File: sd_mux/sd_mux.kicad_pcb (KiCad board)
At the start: 2 copper layers, 77.5 x 38.1 mm, 16 parts, among them IC1 SN74CBT3257DR, IC2 SN74CBT3257DR, J1 Micro_SD_Card_Det, J2 DEVICE 1, J3 DEVICE 2, J4 CONTROL

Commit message: routed
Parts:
- moved R4 44.7 mm to (148.6, 73.7)
- moved LED2 44.7 mm to (153.7, 73.7)
- moved R3 44.6 mm to (148.6, 77.5)
- moved LED1 44.6 mm to (153.7, 77.5)
- moved J4 43.2 mm to (158.8, 83.8)
- moved R1 43.2 mm to (160.0, 87.6)
- moved C1 34.2 mm to (133.3, 72.4), turned to 180 degrees
- moved J1 27.9 mm to (113.0, 72.4)
- moved R5 27.7 mm to (133.3, 108.0), turned to 180 degrees
- moved IC1 23.4 mm to (133.3, 80.0), turned to 270 degrees
- moved IC2 18.0 mm to (133.3, 100.3), turned to 270 degrees
- moved J3 15.3 mm to (110.5, 99.1)
- moved J2 12.0 mm to (161.3, 99.1)
- moved C2 11.4 mm to (133.3, 92.7), turned to 180 degrees
- moved C3 10.5 mm to (121.9, 73.7)
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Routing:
- net GND: track 0.00 -> 241.5 mm, vias 0 -> 18
- net DAT2_1: track 0.00 -> 56.2 mm, vias 0 -> 2
- net VCC: track 13.9 -> 70.1 mm
- net DAT3/CD_1: track 0.00 -> 53.2 mm, vias 0 -> 2
- net Net-(IC1-Pad4): track 68.1 -> 19.2 mm
- net VDD_1: track 0.00 -> 44.3 mm, vias 0 -> 2
- net CMD_1: track 0.00 -> 40.2 mm, vias 0 -> 2
- net Net-(IC1-Pad7): track 56.5 -> 21.9 mm
- net DAT1_2: track 0.00 -> 32.1 mm, vias 0 -> 2
- net DAT0_2: track 0.00 -> 25.9 mm, vias 0 -> 2
- net Net-(IC1-Pad9): track 52.4 -> 31.8 mm, vias 0 -> 2
- net CLK_2: track 0.00 -> 20.6 mm, vias 0 -> 2
- net VDD_2: track 22.7 -> 40.3 mm, vias 2 -> 4
- net OE: track 43.4 -> 27.8 mm, vias 3 -> 2
- net Net-(IC2-Pad12): track 32.2 -> 47.5 mm, vias 2 -> 4
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- added copper zone on B.Cu, net GND
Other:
- board size 77.5 x 38.1 mm -> 63.5 x 38.1 mm

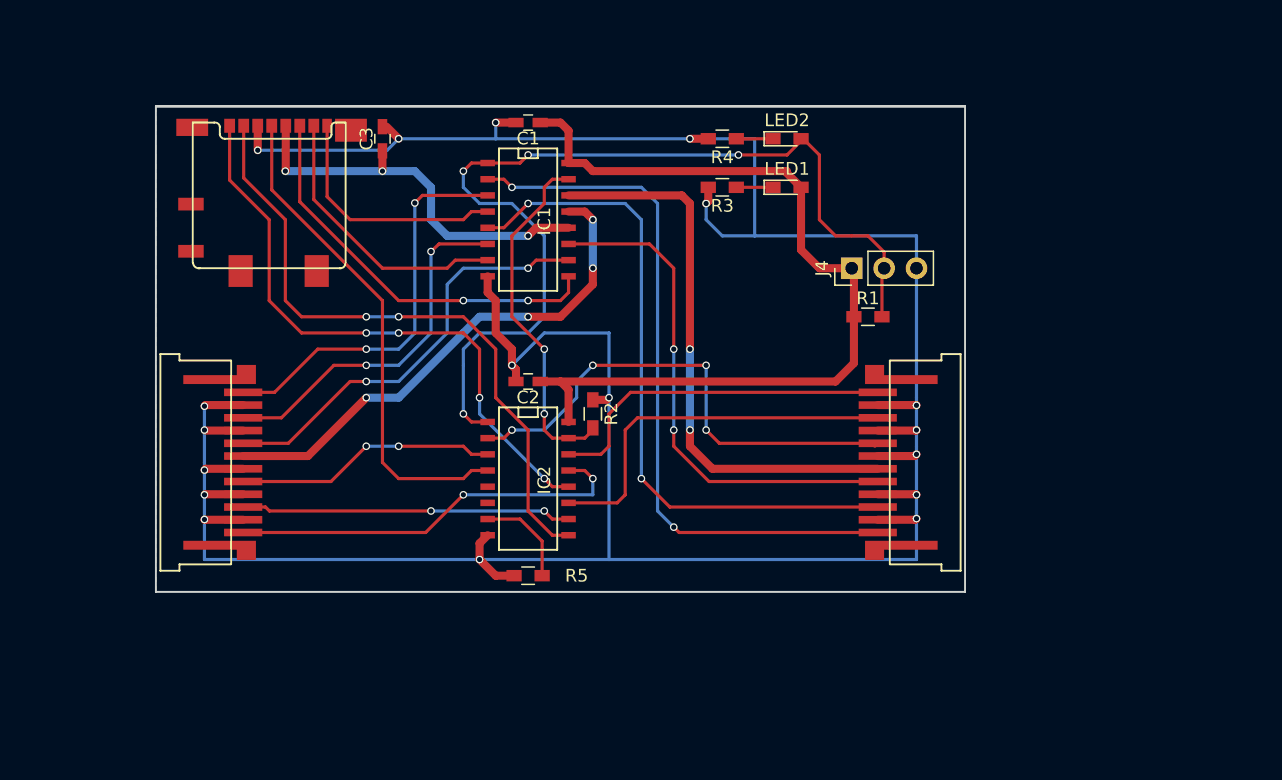
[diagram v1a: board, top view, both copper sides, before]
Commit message: redid the mux board in the same form factor as the beaglebone black, started work on sd plug board
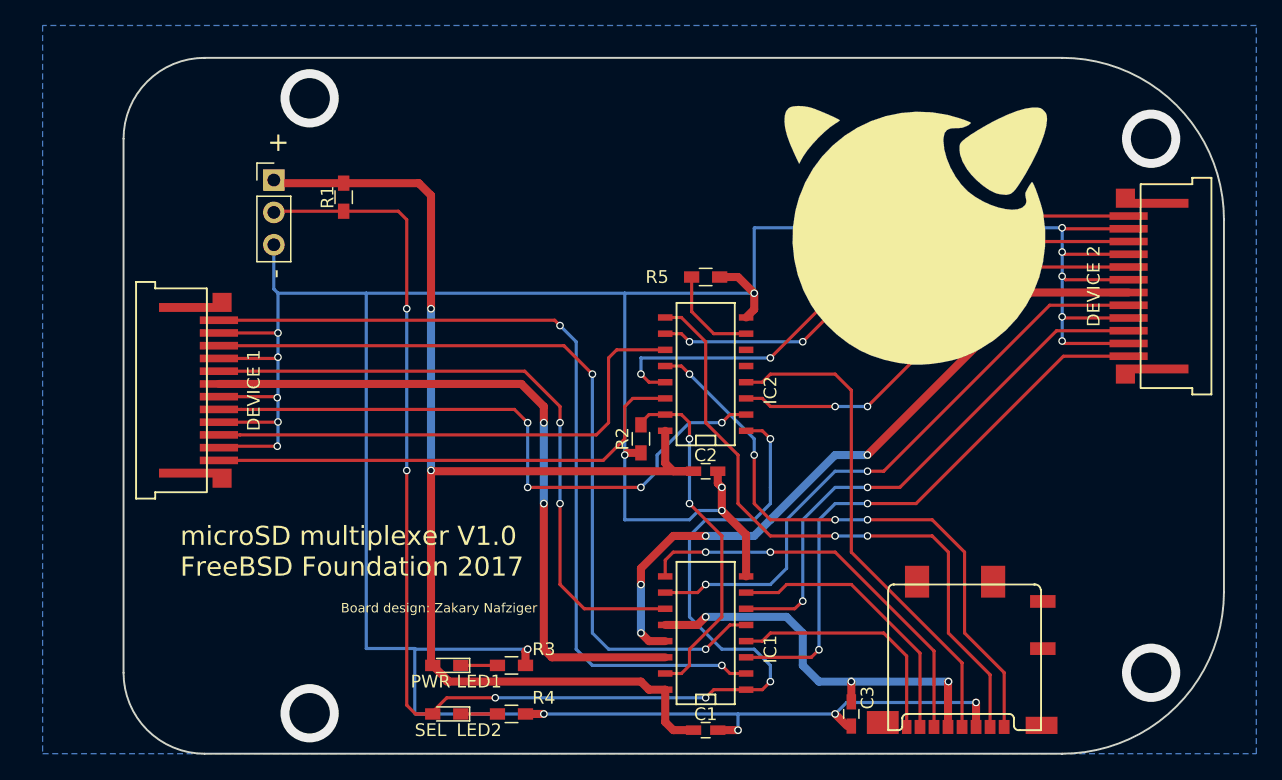
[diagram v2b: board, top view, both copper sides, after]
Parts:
- added G***: LOGO, sd_mux_footprints:fbsd_logo, B.Cu at (146.1, 94.0)
- added G***: LOGO, sd_mux_footprints:fbsd_logo, F.Cu at (163.8, 81.3)
- moved J1 72.5 mm to (167.6, 120.1), turned to 0 degrees
- moved J3 71.8 mm to (181.0, 85.2), turned to 90 degrees
- moved C3 58.2 mm to (158.7, 118.8), turned to 270 degrees
- moved J2 53.0 mm to (108.6, 93.4), turned to 270 degrees
- moved LED2 52.4 mm to (127.0, 118.8), turned to 180 degrees
- moved C1 49.7 mm to (147.3, 120.1), turned to 0 degrees
- moved R4 48.1 mm to (132.0, 118.8), turned to 0 degrees
- moved LED1 46.1 mm to (127.0, 115.0), turned to 180 degrees
- moved J4 45.9 mm to (113.4, 76.9), turned to 0 degrees
- moved R1 42.2 mm to (118.9, 78.2), turned to 270 degrees
- moved R3 41.0 mm to (132.0, 115.0), turned to 0 degrees
- moved IC1 35.3 mm to (147.3, 112.5), turned to 90 degrees
- moved R5 27.3 mm to (147.3, 84.5), turned to 0 degrees
- moved IC2 16.2 mm to (147.3, 92.1), turned to 90 degrees
- moved C2 15.6 mm to (147.3, 99.8), turned to 0 degrees
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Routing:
- net GND: track 241.5 -> 282.1 mm, vias 18 -> 19
- net device_select: track 76.2 -> 109.2 mm, vias 4 -> 6
- net VCC: track 70.1 -> 99.8 mm, vias 0 -> 2
- net VDD_2: track 40.3 -> 54.5 mm
- net DAT2_2: track 31.6 -> 45.8 mm
- net DAT1_2: track 32.1 -> 46.3 mm
- net CLK_2: track 20.6 -> 34.8 mm
- net DAT3/CD_2: track 28.6 -> 42.8 mm
- net CMD_2: track 33.7 -> 47.9 mm
- net DAT0_2: track 25.9 -> 39.9 mm
- net DAT0_1: track 30.0 -> 40.8 mm
- net VDD_1: track 44.3 -> 55.1 mm
- net CMD_1: track 40.2 -> 50.9 mm
- net DAT1_1: track 27.8 -> 38.5 mm
- net DAT2_1: track 56.2 -> 67.0 mm
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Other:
- board size 63.5 x 38.1 mm -> 86.4 x 54.6 mm
- rule pad_to_mask_clearance: 0.2 -> 0
- board text added: "+"
- board text added: "-"
- board text added: "Board design: Zakary Nafziger"
- board text added: "microSD multiplexer V1.0 FreeBSD Foundation 2017"

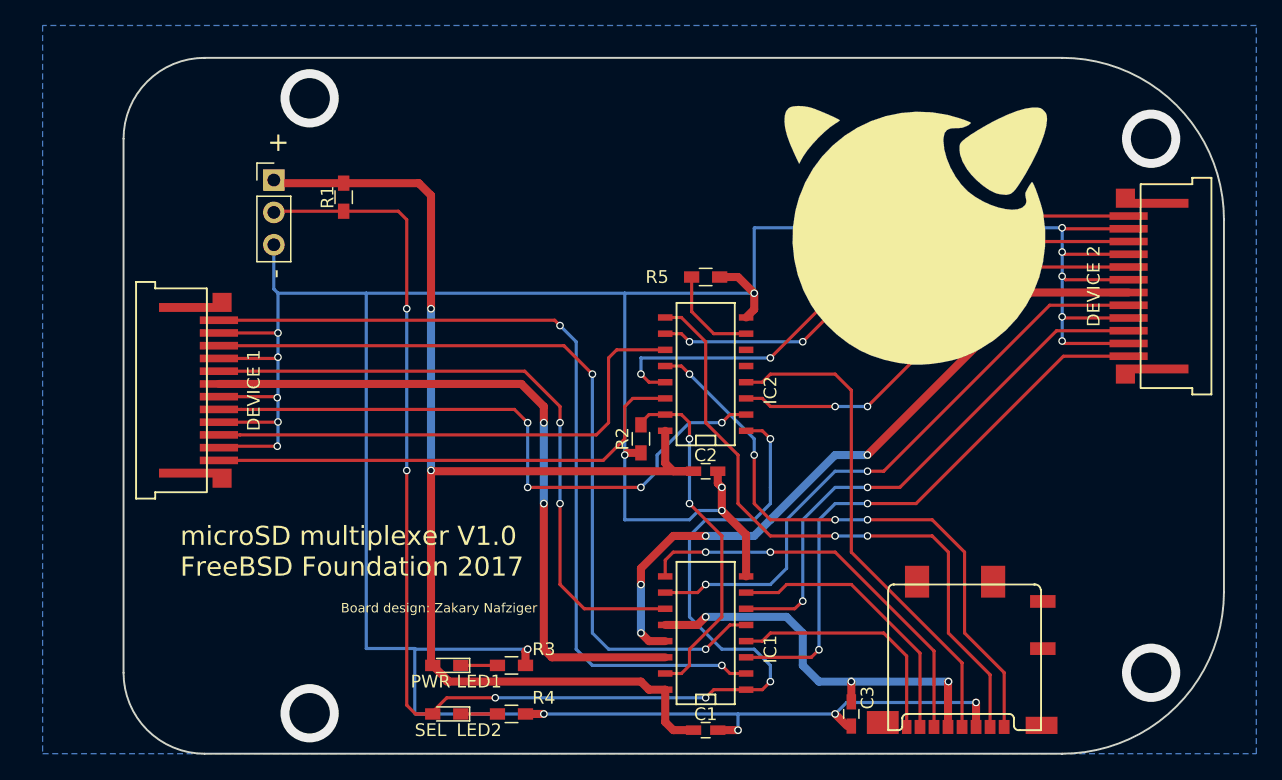
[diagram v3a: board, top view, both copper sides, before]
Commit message: redid mounting holes on mux board
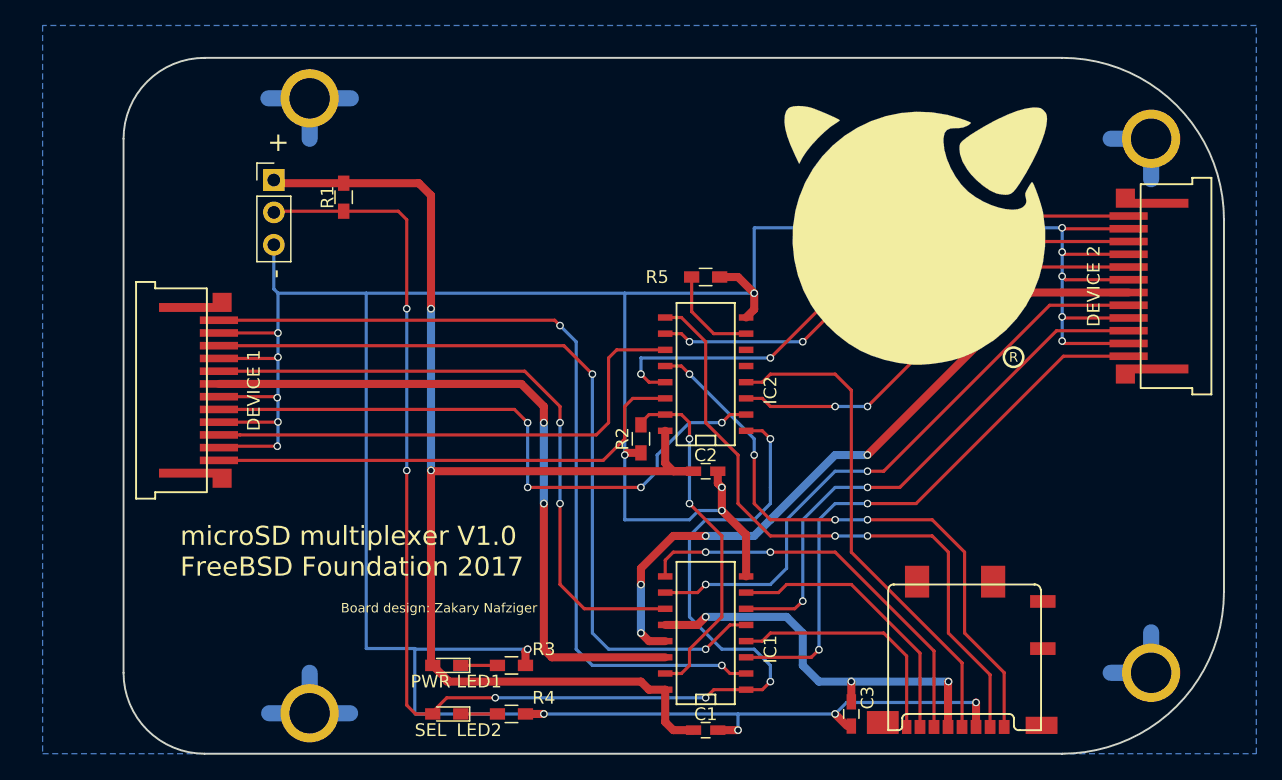
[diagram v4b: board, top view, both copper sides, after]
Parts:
- added REF**: 125mil_plated_mounting_hole, sd_mux_footprints:125mil_plated_mounting_hole, F.Cu at (182.2, 73.7)
- added REF**: 125mil_plated_mounting_hole, sd_mux_footprints:125mil_plated_mounting_hole, F.Cu at (182.2, 115.6)
- added REF**: 125mil_plated_mounting_hole, sd_mux_footprints:125mil_plated_mounting_hole, F.Cu at (116.2, 118.7)
- added REF**: 125mil_plated_mounting_hole, sd_mux_footprints:125mil_plated_mounting_hole, F.Cu at (116.2, 70.5)
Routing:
- net (no net): track 0.00 -> 31.9 mm, vias 4 -> 0
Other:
- rule pad_to_mask_clearance: 0 -> 0.127
- board text added: "R"
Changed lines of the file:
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@@
 (kicad_pcb (version 4) (host pcbnew 4.0.7)
   (general
-    (links 57)
+    (links 0)
     (no_connects 0)
-    (area 101.524999 67.234999 188.035001 121.995001)
+    (area 95.25 64.77 193.614049 122.87)
     (thickness 1.6)
-    (drawings 12)
-    (tracks 385)
+    (drawings 16)
+    (tracks 391)
     (zones 0)
-    (modules 18)
+    (modules 22)
     (nets 31)
   )
@@
   )
   (setup
-    (last_trace_width 0.25)
+    (last_trace_width 1.27)
     (user_trace_width 0.635)
+    (user_trace_width 1.27)
     (trace_clearance 0.25)
     (zone_clearance 0.508)
@@
     (uvia_drill 0.1)
     (uvias_allowed no)
-    (uvia_min_size 0.2)
-    (uvia_min_drill 0.1)
+    (uvia_min_size 0)
+    (uvia_min_drill 0)
     (pcb_text_width 0.3)
     (pcb_text_size 1.5 1.5)
@@
     (pad_size 1.524 1.524)
     (pad_drill 0.762)
-    (pad_to_mask_clearance 0)
+    (pad_to_mask_clearance 0.127)
     (solder_mask_min_width 0.0254)
     (aux_axis_origin 0 0)
@@
       (padsonsilk false)
       (subtractmaskfromsilk false)
-      (outputformat 1)
+      (outputformat 4)
       (mirror false)
       (drillshape 0)
       (scaleselection 1)
-      (outputdirectory gerbers/))
+      (outputdirectory ../../pdfs/sd_mux/))
   )
   (net 0 "")
@@
     (add_net device_select)
   )
+  (module sd_mux_footprints:125mil_plated_mounting_hole (layer F.Cu)
+    (at 182.245 73.66)
+    (fp_text reference REF** (at 0 3) (layer F.SilkS) hide
+      (effects (font (size 1 1) (thickness 0.15)))
+    )
+    (fp_text value 125mil_plated_mounting_hole (at 0 -3) (layer F.Fab)
+      (effects (font (size 1 1) (thickness 0.15)))
+    )
+    (pad 1 thru_hole circle (at 0 0) (size 4.572 4.572) (drill 3.175) (layers *.Cu *.Mask))
+  )
+  (module sd_mux_footprints:125mil_plated_mounting_hole (layer F.Cu)
+    (at 182.245 115.57)
+    (fp_text reference REF** (at 0 3) (layer F.SilkS) hide
+      (effects (font (size 1 1) (thickness 0.15)))
+    )
+    (fp_text value 125mil_plated_mounting_hole (at 0 -3) (layer F.Fab)
+      (effects (font (size 1 1) (thickness 0.15)))
+    )
+    (pad 1 thru_hole circle (at 0 0) (size 4.572 4.572) (drill 3.175) (layers *.Cu *.Mask))
+  )
+  (module sd_mux_footprints:125mil_plated_mounting_hole (layer F.Cu)
+    (at 116.205 118.745)
+    (fp_text reference REF** (at 0 3) (layer F.SilkS) hide
+      (effects (font (size 1 1) (thickness 0.15)))
+    )
+    (fp_text value 125mil_plated_mounting_hole (at 0 -3) (layer F.Fab)
+      (effects (font (size 1 1) (thickness 0.15)))
+    )
+    (pad 1 thru_hole circle (at 0 0) (size 4.572 4.572) (drill 3.175) (layers *.Cu *.Mask))
+  )
   (module sd_mux_footprints:fbsd_logo (layer B.Cu)
     (at 146.05 93.98 180)
@@
       (xy -9.657279 -10.166238) (xy -9.282257 -10.193894) (xy -8.854976 -10.171624)) (layer F.SilkS) (width 0.01))
   )
+  (module sd_mux_footprints:125mil_plated_mounting_hole (layer F.Cu)
+    (at 116.205 70.485)
+    (fp_text reference REF** (at 0 3) (layer F.SilkS) hide
+      (effects (font (size 1 1) (thickness 0.15)))
+    )
+    (fp_text value 125mil_plated_mounting_hole (at 0 -3) (layer F.Fab)
+      (effects (font (size 1 1) (thickness 0.15)))
+    )
+    (pad 1 thru_hole circle (at 0 0) (size 4.572 4.572) (drill 3.175) (layers *.Cu *.Mask))
+  )
+  (gr_text R (at 138.43 103.505) (layer B.SilkS)
+    (effects (font (size 0.762 0.762) (thickness 0.1905)) (justify mirror))
+  )
+  (gr_circle (center 138.43 103.505) (end 137.668 103.505) (layer B.SilkS) (width 0.2))
+  (gr_circle (center 171.45 90.805) (end 170.688 90.805) (layer F.SilkS) (width 0.2))
+  (gr_text R (at 171.45 90.805) (layer F.SilkS)
+    (effects (font (size 0.762 0.762) (thickness 0.1905)))
+  )
   (gr_text "Board design: Zakary Nafziger" (at 126.365 110.49) (layer F.SilkS)
     (effects (font (size 0.738 0.738) (thickness 0.1845)))
@@
     (effects (font (size 1.5 1.5) (thickness 0.3)))
   )
-  (via (at 182.245 73.66) (size 4.572) (drill 3.175) (layers F.Cu B.Cu) (net 0))
-  (via (at 182.245 115.57) (size 4.572) (drill 3.175) (layers F.Cu B.Cu) (net 0))
-  (via (at 116.205 118.745) (size 4.572) (drill 3.175) (layers F.Cu B.Cu) (net 0))
-  (via (at 116.205 70.485) (size 4.572) (drill 3.175) (layers F.Cu B.Cu) (net 0))
+  (segment (start 182.245 73.66) (end 182.245 76.835) (width 1.27) (layer B.Cu) (net 0))
+  (segment (start 182.245 73.66) (end 179.07 73.66) (width 1.27) (layer B.Cu) (net 0))
+  (segment (start 182.245 115.57) (end 182.245 112.395) (width 1.27) (layer B.Cu) (net 0))
+  (segment (start 182.245 115.57) (end 179.07 115.57) (width 1.27) (layer B.Cu) (net 0))
+  (segment (start 116.205 118.745) (end 119.38 118.745) (width 1.27) (layer B.Cu) (net 0))
+  (segment (start 116.205 118.745) (end 116.205 115.57) (width 1.27) (layer B.Cu) (net 0))
+  (segment (start 116.205 118.745) (end 113.03 118.745) (width 1.27) (layer B.Cu) (net 0))
+  (segment (start 116.205 70.485) (end 116.205 73.66) (width 1.27) (layer B.Cu) (net 0))
+  (segment (start 116.205 70.485) (end 119.437892 70.485) (width 1.27) (layer B.Cu) (net 0))
+  (segment (start 116.205 70.485) (end 112.972108 70.485) (width 1.27) (layer B.Cu) (net 0))
   (segment (start 125.73 78.105) (end 124.771778 77.146778) (width 0.635) (layer F.Cu) (net 1))
   (segment (start 124.771778 77.146778) (end 118.876266 77.146778) (width 0.635) (layer F.Cu) (net 1))

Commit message: rerouted mux board to fix FFC flip issue and fix tracks that had become unalaigned from the grid
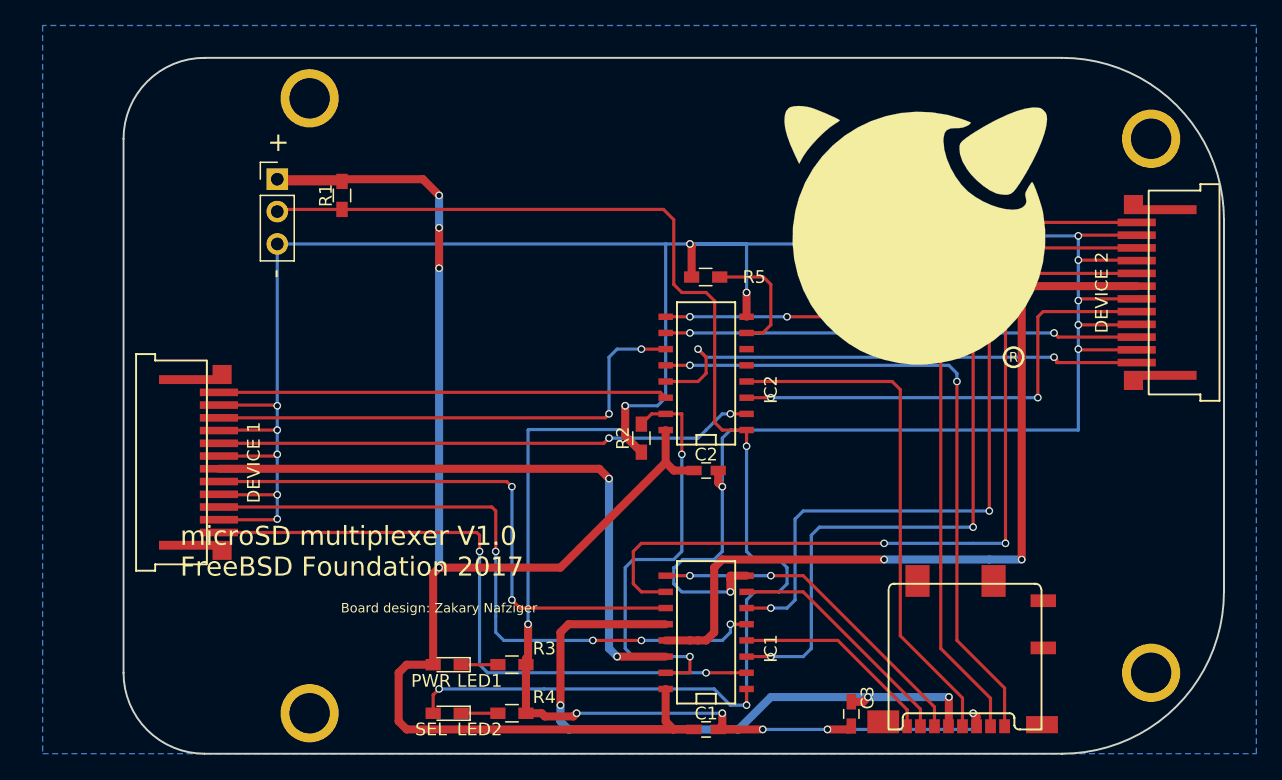
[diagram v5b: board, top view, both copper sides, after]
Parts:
- moved J2 5.66 mm to (108.6, 99.1)
- moved J3 0.81 mm to (181.6, 85.7)
- moved G*** 0.63 mm to (146.1, 94.6)
- moved J4 0.28 mm to (113.7, 76.8)
- moved R1 0.19 mm to (118.7, 78.1)
- moved R2 0.07 mm to (142.2, 97.2)
- moved R3 0.07 mm to (132.1, 114.9)
- moved R4 0.07 mm to (132.1, 118.7)
- moved LED1 0.07 mm to (127.0, 114.9)
- moved LED2 0.07 mm to (127.0, 118.7)
- moved C1 0.07 mm to (147.3, 120.0)
- moved C2 0.07 mm to (147.3, 99.7)
- moved IC1 0.07 mm to (147.3, 112.4)
- moved IC2 0.07 mm to (147.3, 92.1)
- moved J1 0.07 mm to (167.6, 120.0)
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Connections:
- J2 pad 1: DAT2_1 -> DAT1_1
- J2 pad 10: DAT0_1 -> DAT3/CD_1
- J2 pad 12: DAT1_1 -> DAT2_1
- J2 pad 3: DAT3/CD_1 -> DAT0_1
- J2 pad 5: CMD_1 -> CLK_1
- J2 pad 6: VDD_1 -> GND
- J2 pad 7: GND -> VDD_1
- J2 pad 8: CLK_1 -> CMD_1
- J3 pad 1: DAT2_2 -> DAT1_2
- J3 pad 10: DAT0_2 -> DAT3/CD_2
- J3 pad 12: DAT1_2 -> DAT2_2
- J3 pad 3: DAT3/CD_2 -> DAT0_2
- J3 pad 5: CMD_2 -> CLK_2
- J3 pad 6: VDD_2 -> GND
- J3 pad 7: GND -> VDD_2
- J3 pad 8: CLK_2 -> CMD_2
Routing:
- net (no net): track 31.9 -> 0.00 mm
- net GND: track 282.1 -> 303.0 mm, vias 19 -> 21
- net Net-(C3-Pad1): track 31.2 -> 51.1 mm
- net CMD_2: track 47.9 -> 66.2 mm
- net DAT2_2: track 45.8 -> 63.7 mm
- net VCC: track 99.8 -> 115.3 mm, vias 2 -> 4
- net DAT3/CD_2: track 42.8 -> 57.9 mm
- net DAT2_1: track 67.0 -> 51.9 mm
- net DAT3/CD_1: track 63.9 -> 52.2 mm, vias 2 -> 4
- net VDD_2: track 54.5 -> 63.7 mm, vias 4 -> 2
- net CLK_1: track 50.0 -> 42.4 mm, vias 4 -> 2
- net CMD_1: track 50.9 -> 44.4 mm
- net OE: track 27.8 -> 34.1 mm
- net VDD_1: track 55.1 -> 49.0 mm
- net DAT1_2: track 46.3 -> 40.6 mm
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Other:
- rule pad_to_mask_clearance: 0.127 -> 0.15

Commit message: finishing details on sd mux board
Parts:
- J1: value Micro_SD_Card_Det -> MICRO SD CARD
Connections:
- REF** pad 1: (no net) -> GND (x4)
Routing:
- net GND: track 303.0 -> 364.7 mm
- net device_select: track 107.1 -> 107.7 mm
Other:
- rule pad_to_mask_clearance: 0.15 -> 0.127
